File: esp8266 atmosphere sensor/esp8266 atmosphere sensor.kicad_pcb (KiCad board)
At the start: 2 copper layers, 52.7 x 47.6 mm, 61 parts, among them J1 Conn_02x03_Odd_Even, J10 Conn_01x03, J11 Conn_01x03, J12 Conn_01x03, J13 Conn_01x03, J14 Conn_01x03, J2 UJ2-MIBH-G-SMT-TR, J3 LUX sensor, J4 bme280, J5 PIR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

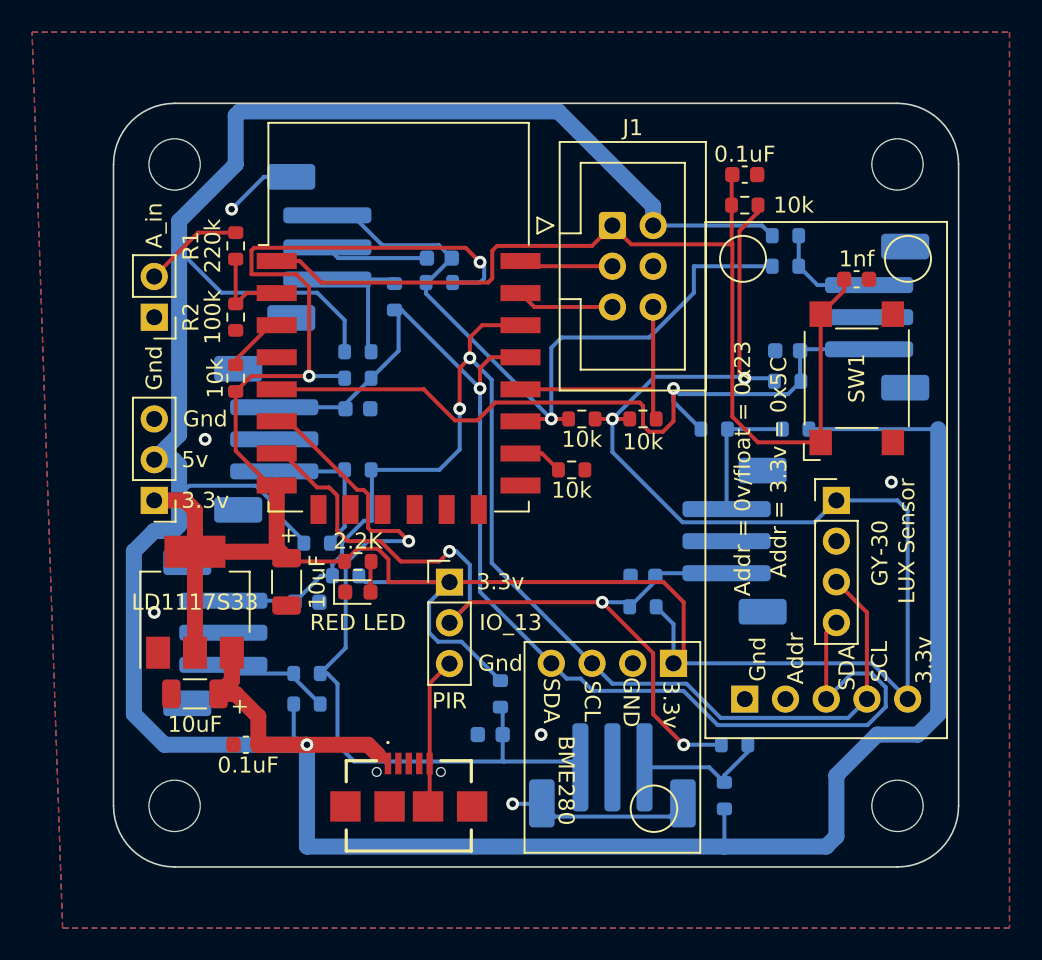
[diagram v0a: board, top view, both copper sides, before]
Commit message: updated footprints
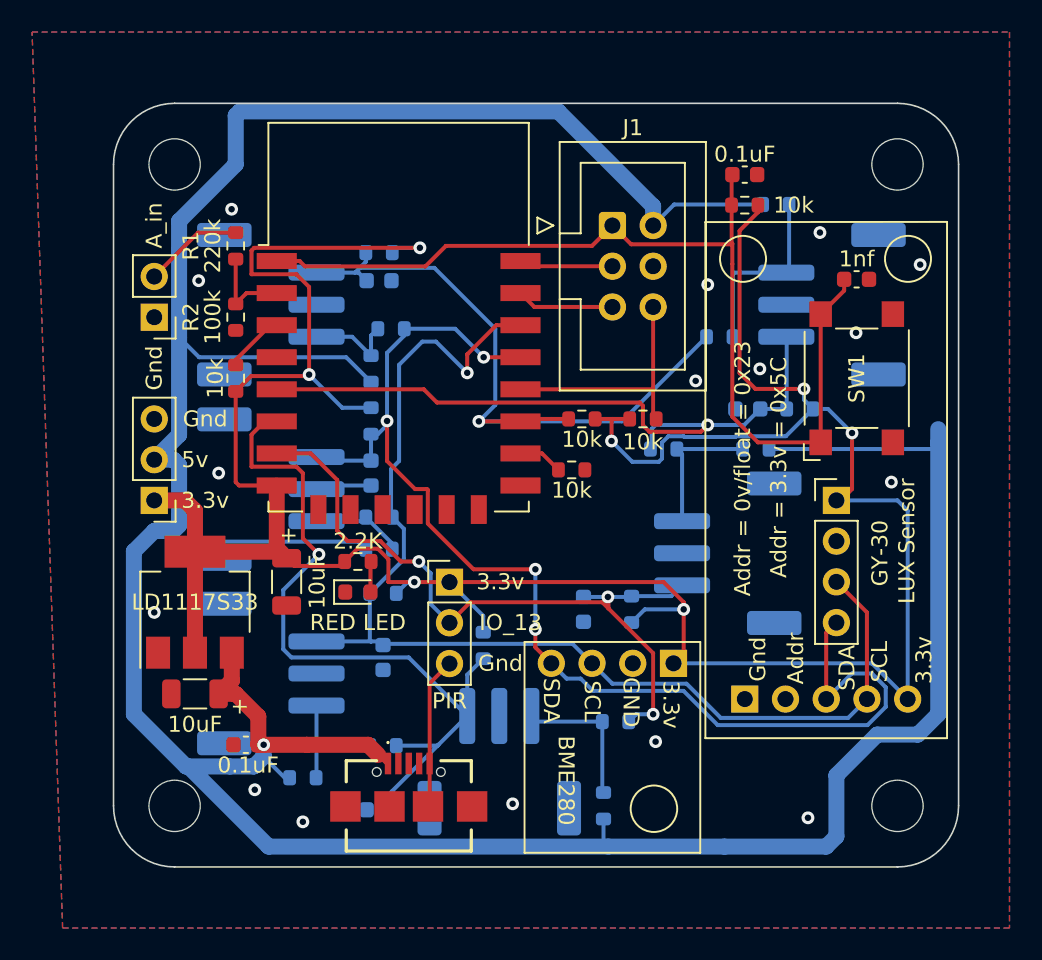
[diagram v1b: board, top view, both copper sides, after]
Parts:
- J10, J11, J12, J13, J14, J9: footprint Connector_JST:JST_PH_B3B-PH-SM4-TB_1x03-1MP_P2.00mm_Vertical -> Connector_JST:JST_PH_S3B-PH-SM4-TB_1x03-1MP_P2.00mm_Horizontal
- moved G*** 22.6 mm to (35.0, 38.2)
- moved C7 8.37 mm to (12.8, 40.2)
- moved R15 7.57 mm to (26.8, 40.0)
- moved R16 7.56 mm to (27.5, 34.8), turned to 0 degrees
- moved J11 7.11 mm to (20.2, 37.2), turned to 180 degrees
- moved R13 6.54 mm to (13.0, 36.2)
- moved R22 6.01 mm to (34.0, 10.8)
- moved C6 5.86 mm to (13.0, 30.8), turned to -90 degrees
- moved J9 4.68 mm to (6.00, 8.75), turned to 90 degrees
- moved R12 4.60 mm to (8.00, 38.2)
- moved C10 4.40 mm to (35.8, 15.2)
- moved J10 4.29 mm to (6.00, 31.8), turned to 90 degrees
- moved C8 4.25 mm to (25.5, 27.8), turned to -90 degrees
- moved R7 4.20 mm to (12.8, 5.50)
- moved C11 4.09 mm to (12.2, 19.2), turned to -90 degrees
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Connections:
- J10 pad 1: /ESP_IO5 -> Net-(R12-Pad2)
- J10 pad 3: Net-(J10-Pad3) -> /ESP_IO5
- J11 pad 1: /ESP_IO12 -> Net-(R15-Pad2)
- J11 pad 3: Net-(J11-Pad3) -> /ESP_IO12
- J12 pad 1: /ESP_IO13 -> Net-(R18-Pad2)
- J12 pad 3: Net-(J12-Pad3) -> /ESP_IO13
- J13 pad 1: /ESP_IO14 -> Net-(R21-Pad2)
- J13 pad 3: Net-(J13-Pad3) -> /ESP_IO14
- J14 pad 1: /ESP_IO4 -> Net-(R24-Pad2)
- J14 pad 3: Net-(J14-Pad3) -> /ESP_IO4
- J9 pad 1: /ESP_IO2 -> Net-(R4-Pad2)
- J9 pad 3: Net-(J9-Pad3) -> /ESP_IO2
- R12 pad 2: Net-(J10-Pad3) -> Net-(R12-Pad2)
- R13 pad 1: Net-(J10-Pad3) -> Net-(R12-Pad2)
- R15 pad 2: Net-(J11-Pad3) -> Net-(R15-Pad2)
- R16 pad 1: Net-(J11-Pad3) -> Net-(R15-Pad2)
- R18 pad 2: Net-(J12-Pad3) -> Net-(R18-Pad2)
- R19 pad 1: Net-(J12-Pad3) -> Net-(R18-Pad2)
- R21 pad 2: Net-(J13-Pad3) -> Net-(R21-Pad2)
- R22 pad 1: Net-(J13-Pad3) -> Net-(R21-Pad2)
- R24 pad 2: Net-(J14-Pad3) -> Net-(R24-Pad2)
- R25 pad 1: Net-(J14-Pad3) -> Net-(R24-Pad2)
- R4 pad 2: Net-(J9-Pad3) -> Net-(R4-Pad2)
- R6 pad 1: Net-(J9-Pad3) -> Net-(R4-Pad2)
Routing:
- net GND: track 31.9 -> 13.0 mm, vias 6 -> 16
- net +3V3: track 190.8 -> 179.1 mm, vias 4 -> 7
- net Net-(R21-Pad2): track 0.00 -> 11.6 mm
- net Net-(J14-Pad3): track 9.24 -> 0.00 mm
- net Net-(R15-Pad2): track 0.00 -> 9.03 mm
- net Net-(R18-Pad2): track 0.00 -> 8.73 mm
- net Net-(J9-Pad3): track 8.44 -> 0.00 mm
- net Net-(J12-Pad3): track 8.44 -> 0.00 mm
- net Net-(J11-Pad3): track 8.33 -> 0.00 mm
- net Net-(R12-Pad2): track 0.00 -> 7.90 mm
- net /ESP_IO13: track 53.2 -> 45.4 mm
- net Net-(J10-Pad3): track 7.20 -> 0.00 mm
- net /ESP_IO5: track 81.6 -> 74.5 mm, vias 2 -> 1
- net Net-(J13-Pad3): track 6.78 -> 0.00 mm
- net Net-(R24-Pad2): track 0.00 -> 5.86 mm
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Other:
- board text added: "Atmosphere sensor board v3"
- board text removed: "Atmosphere sensor board v2"

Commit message: redid layout as 4-layer without moving parts
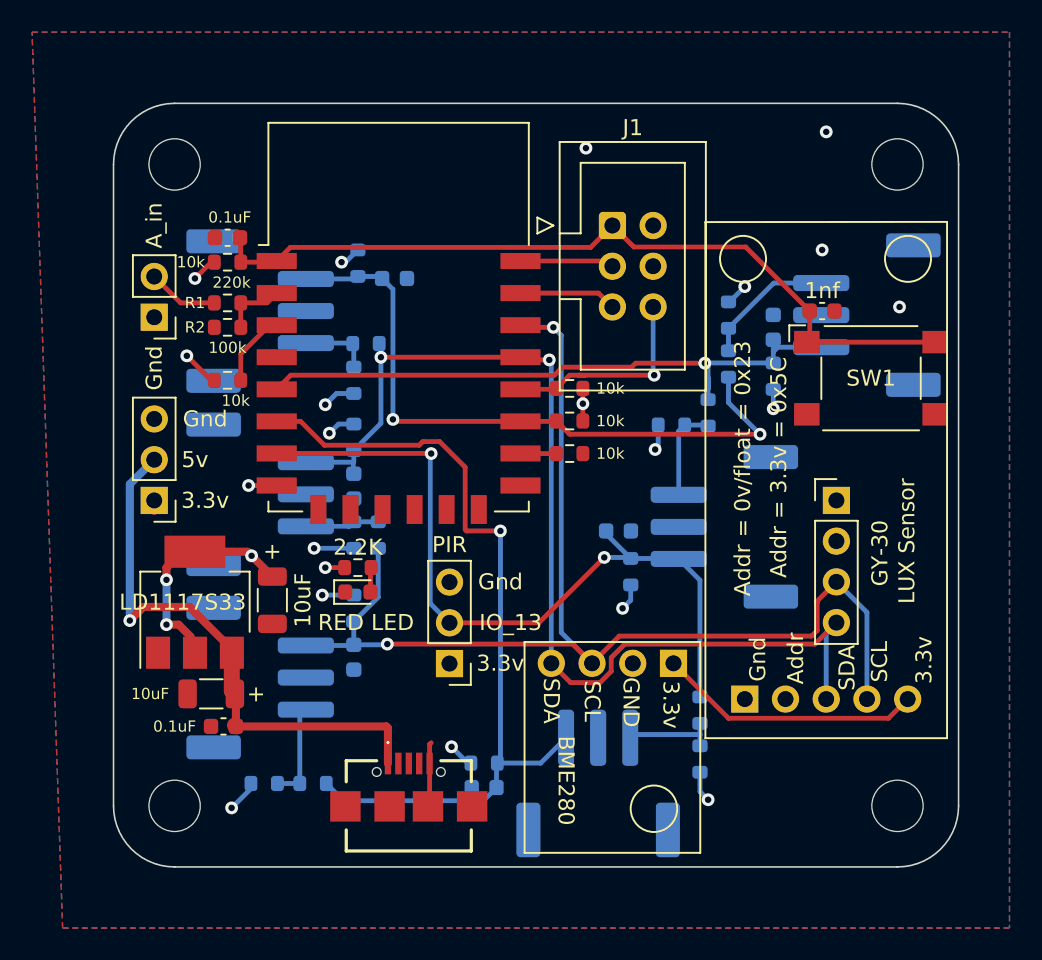
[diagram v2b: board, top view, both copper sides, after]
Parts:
- moved C9 32.5 mm to (3.30, 4.57), turned to 180 degrees
- moved R9 32.5 mm to (3.30, 6.10), turned to 0 degrees
- moved R21 7.50 mm to (34.5, 9.40), turned to -90 degrees
- moved R17 7.34 mm to (19.3, 37.3), turned to 0 degrees
- moved C7 6.70 mm to (19.3, 38.9)
- moved R15 6.69 mm to (32.8, 37.1)
- moved J11 6.31 mm to (26.4, 38.6)
- moved R18 5.47 mm to (31.0, 16.3), turned to 0 degrees
- moved C8 5.36 mm to (27.7, 22.9), turned to 0 degrees
- moved C10 5.33 mm to (37.3, 10.2), turned to 90 degrees
- moved R16 5.31 mm to (32.8, 34.0), turned to 90 degrees
- moved J5 5.08 mm to (17.1, 31.1), turned to 180 degrees
- moved R13 4.96 mm to (8.64, 38.6)
- moved R10 4.95 mm to (24.6, 14.0), turned to 180 degrees
- moved R1 3.59 mm to (3.30, 8.64), turned to 0 degrees
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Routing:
- net +5V: track 219.3 -> 46.7 mm, vias 1 -> 7
- net +3V3: track 179.1 -> 49.1 mm, vias 7 -> 14
- net /ESP_RST: track 62.2 -> 50.2 mm
- net /ESP_IO4: track 76.8 -> 66.7 mm, vias 4 -> 2
- net GND: track 13.0 -> 4.05 mm, vias 16 -> 4
- net /ESP_IO12: track 47.2 -> 51.7 mm
- net /ESP_IO14: track 43.6 -> 39.2 mm
- net Net-(R21-Pad2): track 11.6 -> 8.35 mm
- net Net-(R15-Pad2): track 9.03 -> 5.83 mm
- net /ESP_IO13: track 45.4 -> 48.4 mm, vias 3 -> 2
- net Net-(R18-Pad2): track 8.73 -> 5.99 mm
- net /ESP_IO0: track 15.4 -> 13.4 mm, vias 0 -> 1
- net /ESP_IO2: track 43.4 -> 41.6 mm, vias 1 -> 2
- net /Analog_In: track 6.21 -> 4.43 mm
- net Net-(R12-Pad2): track 7.90 -> 6.16 mm
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- added copper zone on In1.Cu, net +3V3
- added copper zone on In2.Cu, net +5V
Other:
- copper layers 2 -> 4

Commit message: generated gerbers, added gitignore
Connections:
- J10 pad MP: GND -> (no net)
- J11 pad MP: GND -> (no net)
- J12 pad MP: GND -> (no net)
- J13 pad MP: GND -> (no net)
- J14 pad MP: GND -> (no net)
- J9 pad MP: GND -> (no net)
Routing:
- net +3V3: track 49.1 -> 48.1 mm
- net /ESP_IO14: track 39.2 -> 38.6 mm

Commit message: tweaked silk for proper labels
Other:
- board text added: "IO_14"
- board text added: "Recommended values: Cfilter: 30pF Rfilter: 4.7k R5v, red 1.9k R5v, blue 3.9k"
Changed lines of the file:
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@@
     (effects (font (size 0.7 0.7) (thickness 0.1)) (justify mirror))
   )
-  (gr_text "IO_4" (at 46.99 16.764 90) (layer "B.SilkS")
+  (gr_text "IO_14" (at 46.99 16.764 90) (layer "B.SilkS")
     (effects (font (size 1 1) (thickness 0.15)) (justify mirror))
   )
@@
     (effects (font (size 1 1) (thickness 0.15)) (justify mirror))
   )
+  (gr_text "Recommended values:\nCfilter: 30pF\nRfilter: 4.7k\nR5v, red 1.9k\nR5v, blue 3.9k" (at 22.352 15.748) (layer "B.SilkS")
+    (effects (font (size 1 1) (thickness 0.15)) (justify mirror))
+  )

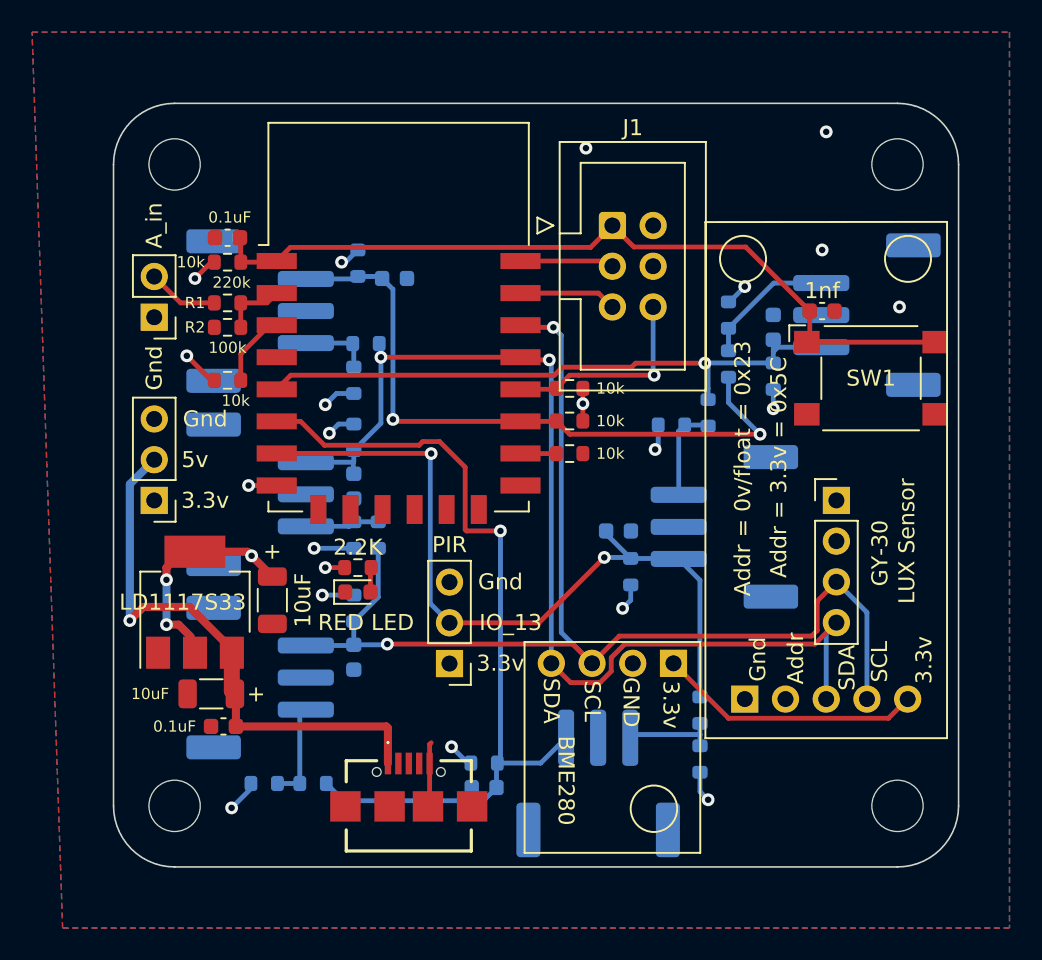
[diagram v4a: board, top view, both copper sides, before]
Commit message: tweaked locations for button connectors
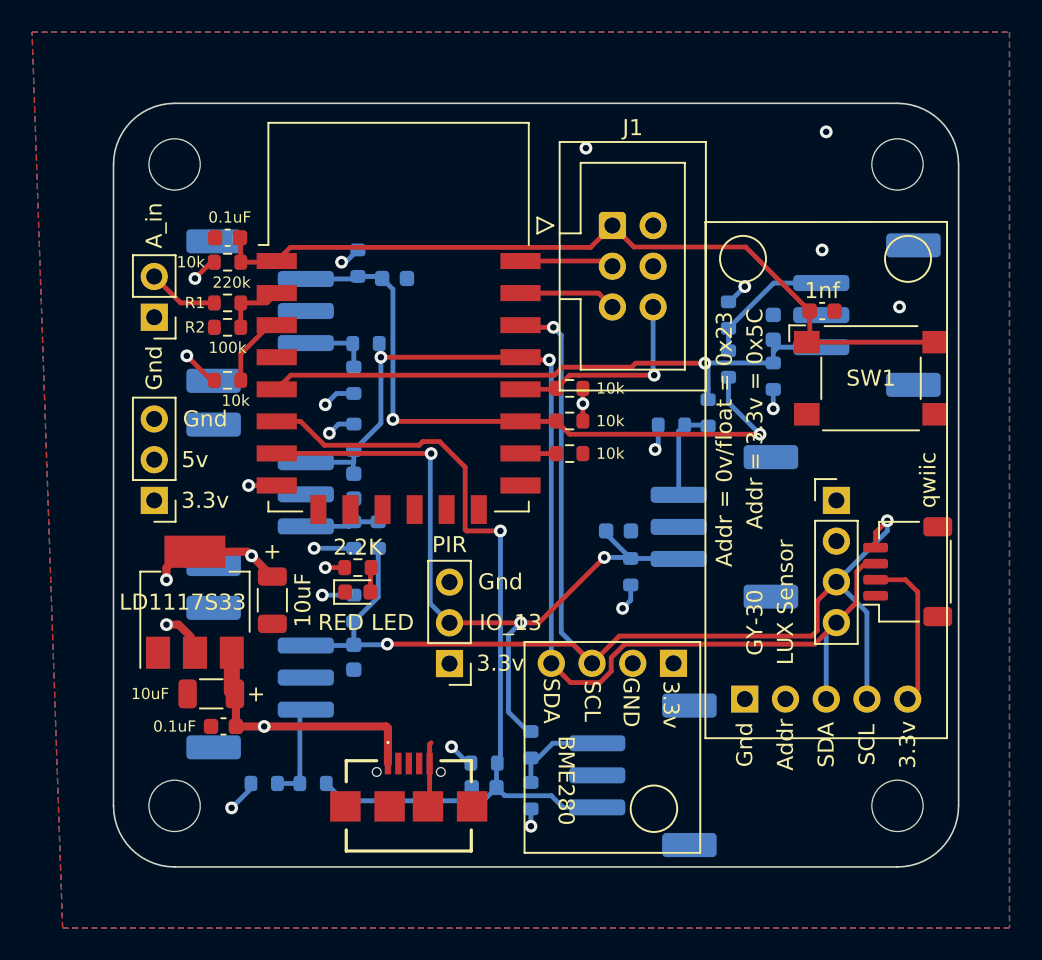
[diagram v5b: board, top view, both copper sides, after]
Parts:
- added J15: qwiic, Connector_JST:JST_SH_SM04B-SRSS-TB_1x04-1MP_P1.00mm_Horizontal, F.Cu at (45.7, 25.4)
- moved R15 10.8 mm to (22.2, 39.4)
- moved R16 10.8 mm to (22.2, 36.2)
- moved J11 2.84 mm to (29.2, 38.1), turned to -90 degrees
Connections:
- J10 pad MP: (no net) -> GND
- J11 pad MP: (no net) -> GND
- J12 pad MP: (no net) -> GND
- J13 pad MP: (no net) -> GND
- J14 pad MP: (no net) -> GND
- J9 pad MP: (no net) -> GND
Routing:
- net +5V: track 46.6 -> 27.3 mm
- net +3V3: track 48.1 -> 38.7 mm
- net /ESP_IO5: track 75.7 -> 82.8 mm, vias 2 -> 3
- net /ESP_IO4: track 66.7 -> 71.8 mm
- net /ESP_IO12: track 51.7 -> 53.6 mm
- net /ESP_IO13: track 48.2 -> 46.9 mm, vias 2 -> 3
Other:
- board text added: "Atmosphere sensor board v3.1"
- board text removed: "Atmosphere sensor board v3"
